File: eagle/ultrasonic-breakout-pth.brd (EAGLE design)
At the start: 58.7 x 41.9 mm, 25 parts, among them Q1 16 MHz, U1 ATMEGA328P_PDIP

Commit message: refining board layout
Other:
- board size 58.7 x 41.9 mm -> 57.5 x 41.9 mm
- board text added: "MISO"
- board text added: "MOSI"
- board text added: "SCK"
- board text added: "SS"
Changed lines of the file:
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@@
 <board>
 <plain>
-<wire x1="1.27" y1="36.83" x2="59.995" y2="36.83" width="0" layer="20"/>
-<wire x1="59.995" y1="36.83" x2="59.995" y2="78.73" width="0" layer="20"/>
-<wire x1="59.995" y1="78.73" x2="1.27" y2="78.73" width="0" layer="20"/>
+<wire x1="1.27" y1="36.83" x2="58.725" y2="36.83" width="0" layer="20"/>
+<wire x1="58.725" y1="36.83" x2="58.725" y2="78.73" width="0" layer="20"/>
+<wire x1="58.725" y1="78.73" x2="1.27" y2="78.73" width="0" layer="20"/>
 <wire x1="1.27" y1="78.73" x2="1.27" y2="36.83" width="0" layer="20"/>
 <hole x="3.81" y="76.2" drill="3.2"/>
 <hole x="3.81" y="39.37" drill="3.2"/>
-<hole x="57.785" y="39.37" drill="3.2"/>
+<hole x="54.61" y="39.37" drill="3.2"/>
 <hole x="55.245" y="76.2" drill="3.2"/>
 <text x="7.62" y="75.565" size="0.6096" layer="25" rot="R90">GND</text>
@@
 <text x="15.24" y="75.565" size="0.6096" layer="25" rot="R90">5V</text>
 <text x="17.78" y="76.835" size="1.016" layer="25" font="vector" ratio="10">HC-SR04 Breakout 1.0.1</text>
-<text x="54.61" y="40.005" size="1.016" layer="25" font="vector" ratio="10" rot="R180">Copyright 2016 Grove Enterprises LLC</text>
+<text x="50.8" y="40.005" size="1.016" layer="25" font="vector" ratio="10" rot="R180">Copyright 2016 Grove Enterprises LLC</text>
+<text x="57.15" y="55.245" size="0.6096" layer="25" rot="R90">5V</text>
+<text x="57.15" y="52.705" size="0.6096" layer="25" rot="R90">SCK</text>
+<text x="57.15" y="49.53" size="0.6096" layer="25" rot="R90">MISO</text>
+<text x="57.15" y="46.99" size="0.6096" layer="25" rot="R90">MOSI</text>
+<text x="57.15" y="45.085" size="0.6096" layer="25" rot="R90">SS</text>
+<text x="57.15" y="42.545" size="0.6096" layer="25" rot="R90">GND</text>
 </plain>
 <attributes>
@@
 <elements>
 <element name="ARDUINO" library="SparkFun-Connectors" package="1X06_LOCK" value="" x="54.61" y="43.18" smashed="yes" rot="R90">
-<attribute name="NAME" x="57.404" y="42.291" size="0.8128" layer="25" rot="R90"/>
+<attribute name="NAME" x="52.324" y="42.291" size="0.8128" layer="25" rot="R90"/>
 <attribute name="VALUE" x="57.404" y="51.181" size="1.27" layer="25" rot="R90"/>
 </element>

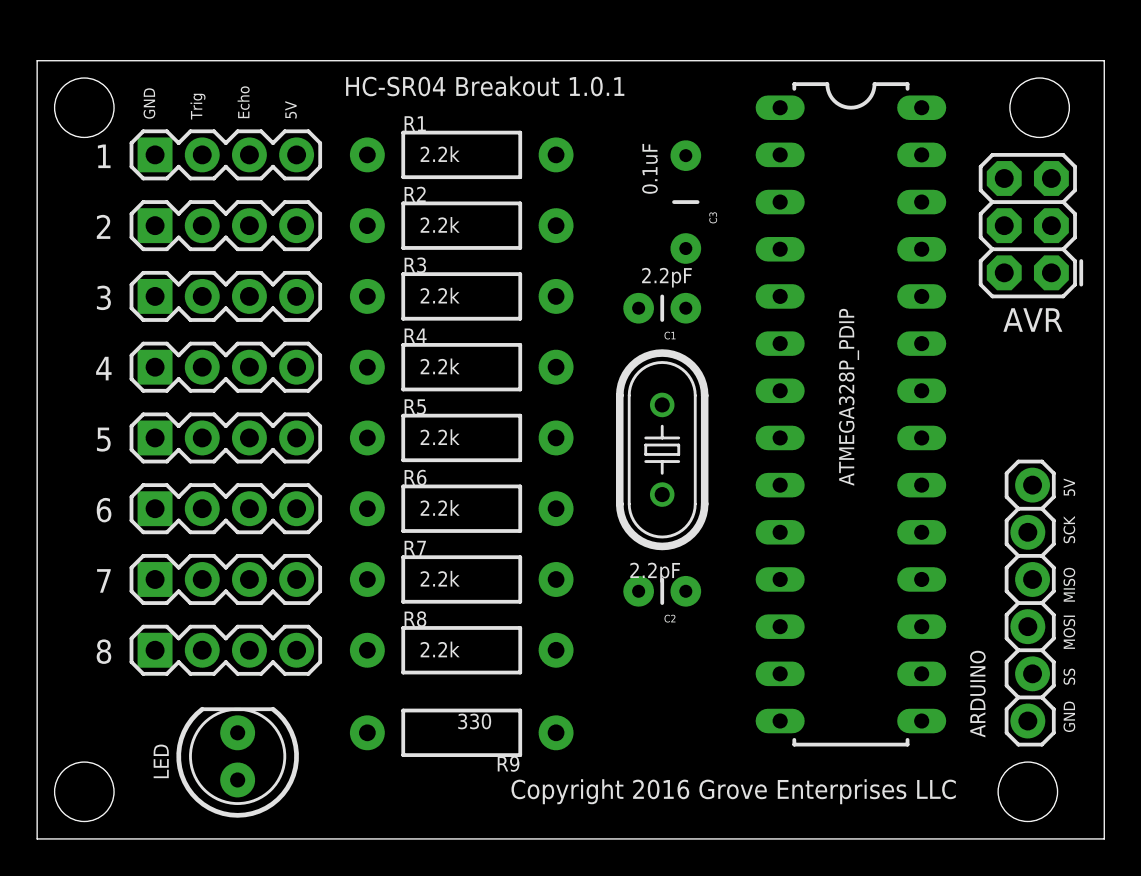
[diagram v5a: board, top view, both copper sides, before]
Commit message: changed first connecter to swap trig/echo
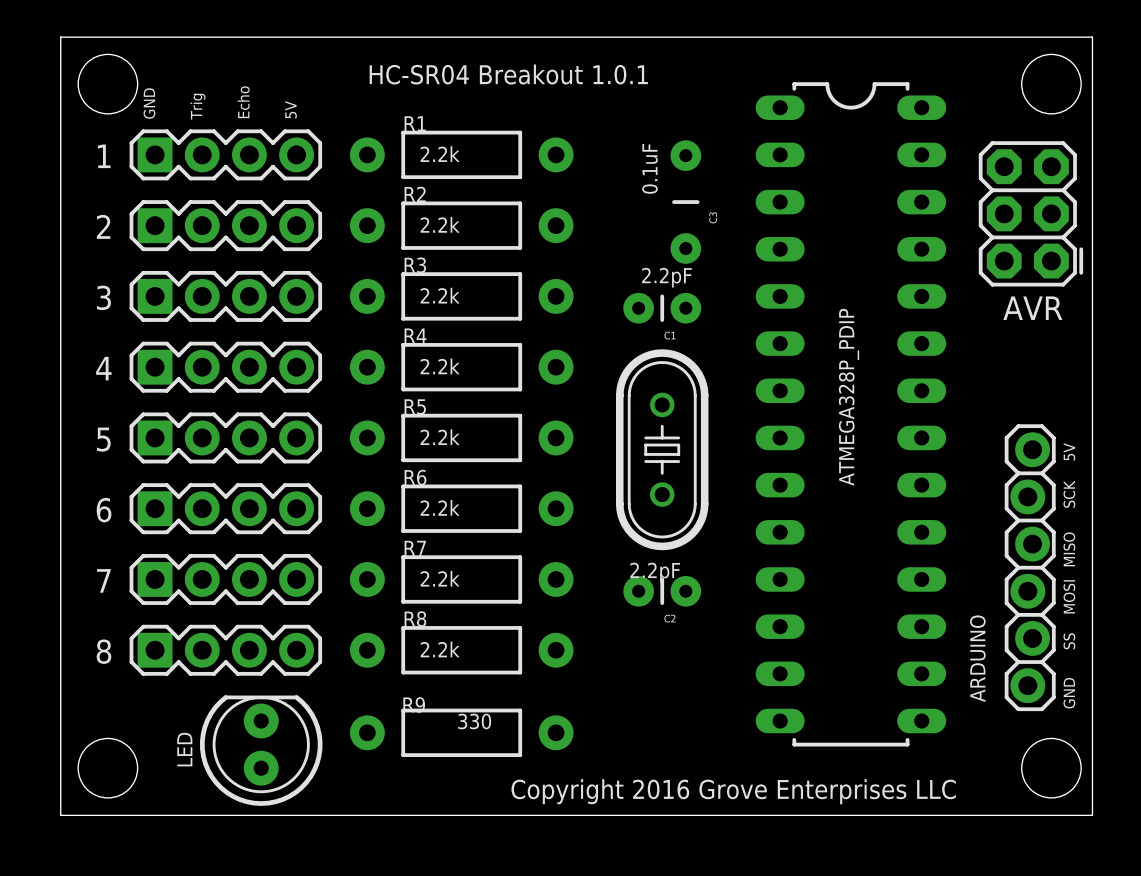
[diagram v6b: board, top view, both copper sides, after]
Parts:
- moved ARDUINO 1.91 mm to (54.6, 45.1)
- moved LED 1.42 mm to (13.3, 41.9)
- moved AVR 0.63 mm to (55.9, 67.9)
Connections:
- removed net TRIGGER1: 1.2, R1.P$1
- new net N$4: 1.3, R1.P$1
- net PD0: now also 1.2; no longer 1.3
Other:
- board size 57.5 x 41.9 mm -> 55.6 x 41.9 mm

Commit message: finished swapping trig/echo on all connectors
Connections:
- net N$10: now also 7.3; no longer 7.2
- net N$11: now also 8.3; no longer 8.2
- net N$5: now also 2.3; no longer 2.2
- net N$6: now also 3.3; no longer 3.2
- net N$7: now also 4.3; no longer 4.2
- net N$8: now also 5.3; no longer 5.2
- net N$9: now also 6.3; no longer 6.2
- net PD1: now also 2.2; no longer 2.3
- net PD2: now also 3.2; no longer 3.3
- net PD3: now also 4.2; no longer 4.3
- net PD4: now also 5.2; no longer 5.3
- net PD5: now also 6.2; no longer 6.3
- net PD6: now also 7.2; no longer 7.3
- net PD7: now also 8.2; no longer 8.3
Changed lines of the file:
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@@
 <hole x="55.88" y="77.47" drill="3.2"/>
 <text x="7.62" y="75.565" size="0.6096" layer="25" rot="R90">GND</text>
-<text x="10.16" y="75.565" size="0.6096" layer="25" rot="R90">Trig</text>
-<text x="12.7" y="75.565" size="0.6096" layer="25" rot="R90">Echo</text>
+<text x="12.7" y="75.565" size="0.6096" layer="25" rot="R90">Trig</text>
+<text x="10.16" y="75.565" size="0.6096" layer="25" rot="R90">Echo</text>
 <text x="15.24" y="75.565" size="0.6096" layer="25" rot="R90">5V</text>
 <text x="19.05" y="77.47" size="1.016" layer="25" font="vector" ratio="10">HC-SR04 Breakout 1.0.1</text>
@@
 <contactref element="2" pad="1"/>
 <contactref element="3" pad="1"/>
-<contactref element="4" pad="1"/>
 <contactref element="5" pad="1"/>
 <contactref element="6" pad="1"/>
@@
 <contactref element="C3" pad="2"/>
 <contactref element="LED" pad="K"/>
+<contactref element="4" pad="1"/>
 <wire x1="48.895" y1="60.96" x2="53.34" y2="73.025" width="0" layer="19" extent="1-1"/>
 <wire x1="41.275" y1="58.42" x2="48.895" y2="60.96" width="0" layer="19" extent="1-1"/>
@@
 <signal name="PD3">
 <contactref element="U1" pad="5"/>
-<contactref element="4" pad="3"/>
 <contactref element="R4" pad="P$2"/>
+<contactref element="4" pad="2"/>
 <wire x1="29.21" y1="62.23" x2="41.275" y2="66.04" width="0" layer="19" extent="1-1"/>
-<wire x1="12.7" y1="62.23" x2="29.21" y2="62.23" width="0" layer="19" extent="1-1"/>
+<wire x1="10.16" y1="62.23" x2="29.21" y2="62.23" width="0" layer="19" extent="1-1"/>
 </signal>
 <signal name="PD4">
 <contactref element="U1" pad="6"/>
-<contactref element="5" pad="3"/>
 <contactref element="R5" pad="P$2"/>
+<contactref element="5" pad="2"/>
 <wire x1="29.21" y1="58.42" x2="41.275" y2="63.5" width="0" layer="19" extent="1-1"/>
-<wire x1="12.7" y1="58.42" x2="29.21" y2="58.42" width="0" layer="19" extent="1-1"/>
+<wire x1="10.16" y1="58.42" x2="29.21" y2="58.42" width="0" layer="19" extent="1-1"/>
 </signal>
 <signal name="PD5">
 <contactref element="U1" pad="11"/>
-<contactref element="6" pad="3"/>
 <contactref element="R6" pad="P$2"/>
+<contactref element="6" pad="2"/>
 <wire x1="29.21" y1="54.61" x2="41.275" y2="50.8" width="0" layer="19" extent="1-1"/>
-<wire x1="12.7" y1="54.61" x2="29.21" y2="54.61" width="0" layer="19" extent="1-1"/>
+<wire x1="10.16" y1="54.61" x2="29.21" y2="54.61" width="0" layer="19" extent="1-1"/>
 </signal>
 <signal name="PD6">
 <contactref element="U1" pad="12"/>
-<contactref element="7" pad="3"/>
 <contactref element="R7" pad="P$2"/>
+<contactref element="7" pad="2"/>
 <wire x1="29.21" y1="50.8" x2="41.275" y2="48.26" width="0" layer="19" extent="1-1"/>
-<wire x1="12.7" y1="50.8" x2="29.21" y2="50.8" width="0" layer="19" extent="1-1"/>
+<wire x1="10.16" y1="50.8" x2="29.21" y2="50.8" width="0" layer="19" extent="1-1"/>
 </signal>
 <signal name="PD7">
 <contactref element="U1" pad="13"/>
-<contactref element="8" pad="3"/>
 <contactref element="R8" pad="P$2"/>
+<contactref element="8" pad="2"/>
 <wire x1="29.21" y1="46.99" x2="41.275" y2="45.72" width="0" layer="19" extent="1-1"/>
-<wire x1="12.7" y1="46.99" x2="29.21" y2="46.99" width="0" layer="19" extent="1-1"/>
+<wire x1="10.16" y1="46.99" x2="29.21" y2="46.99" width="0" layer="19" extent="1-1"/>
 </signal>
 <signal name="PD1">
 <contactref element="U1" pad="3"/>
-<contactref element="2" pad="3"/>
 <contactref element="R2" pad="P$2"/>
+<contactref element="2" pad="2"/>
 <wire x1="29.21" y1="69.85" x2="41.275" y2="71.12" width="0" layer="19" extent="1-1"/>
-<wire x1="12.7" y1="69.85" x2="29.21" y2="69.85" width="0" layer="19" extent="1-1"/>
+<wire x1="10.16" y1="69.85" x2="29.21" y2="69.85" width="0" layer="19" extent="1-1"/>
 </signal>
 <signal name="PD2">
 <contactref element="U1" pad="4"/>
-<contactref element="3" pad="3"/>
 <contactref element="R3" pad="P$2"/>
+<contactref element="3" pad="2"/>
 <wire x1="29.21" y1="66.04" x2="41.275" y2="68.58" width="0" layer="19" extent="1-1"/>
-<wire x1="12.7" y1="66.04" x2="29.21" y2="66.04" width="0" layer="19" extent="1-1"/>
-</signal>
-<signal name="N$5">
-<contactref element="2" pad="2"/>
-<contactref element="R2" pad="P$1"/>
-<wire x1="10.16" y1="69.85" x2="19.05" y2="69.85" width="0" layer="19" extent="1-1"/>
-</signal>
-<signal name="N$6">
-<contactref element="3" pad="2"/>
-<contactref element="R3" pad="P$1"/>
-<wire x1="10.16" y1="66.04" x2="19.05" y2="66.04" width="0" layer="19" extent="1-1"/>
-</signal>
-<signal name="N$7">
-<contactref element="4" pad="2"/>
-<contactref element="R4" pad="P$1"/>
-<wire x1="10.16" y1="62.23" x2="19.05" y2="62.23" width="0" layer="19" extent="1-1"/>
-</signal>
-<signal name="N$8">
-<contactref element="5" pad="2"/>
-<contactref element="R5" pad="P$1"/>
-<wire x1="10.16" y1="58.42" x2="19.05" y2="58.42" width="0" layer="19" extent="1-1"/>
-</signal>
-<signal name="N$9">
-<contactref element="6" pad="2"/>
-<contactref element="R6" pad="P$1"/>
-<wire x1="10.16" y1="54.61" x2="19.05" y2="54.61" width="0" layer="19" extent="1-1"/>
-</signal>
-<signal name="N$10">
-<contactref element="7" pad="2"/>
-<contactref element="R7" pad="P$1"/>
-<wire x1="10.16" y1="50.8" x2="19.05" y2="50.8" width="0" layer="19" extent="1-1"/>
-</signal>
-<signal name="N$11">
-<contactref element="8" pad="2"/>
-<contactref element="R8" pad="P$1"/>
-<wire x1="10.16" y1="46.99" x2="19.05" y2="46.99" width="0" layer="19" extent="1-1"/>
+<wire x1="10.16" y1="66.04" x2="29.21" y2="66.04" width="0" layer="19" extent="1-1"/>
 </signal>
 <signal name="N$12">
@@
 <wire x1="12.7" y1="73.66" x2="19.05" y2="73.66" width="0" layer="19" extent="1-1"/>
 </signal>
+<signal name="N$5">
+<contactref element="2" pad="3"/>
+<contactref element="R2" pad="P$1"/>
+<wire x1="12.7" y1="69.85" x2="19.05" y2="69.85" width="0" layer="19" extent="1-1"/>
+</signal>
+<signal name="N$6">
+<contactref element="3" pad="3"/>
+<contactref element="R3" pad="P$1"/>
+<wire x1="12.7" y1="66.04" x2="19.05" y2="66.04" width="0" layer="19" extent="1-1"/>
+</signal>
+<signal name="N$7">
+<contactref element="4" pad="3"/>
+<contactref element="R4" pad="P$1"/>
+<wire x1="12.7" y1="62.23" x2="19.05" y2="62.23" width="0" layer="19" extent="1-1"/>
+</signal>
+<signal name="N$8">
+<contactref element="5" pad="3"/>
+<contactref element="R5" pad="P$1"/>
+<wire x1="12.7" y1="58.42" x2="19.05" y2="58.42" width="0" layer="19" extent="1-1"/>
+</signal>
+<signal name="N$9">
+<contactref element="6" pad="3"/>
+<contactref element="R6" pad="P$1"/>
+<wire x1="12.7" y1="54.61" x2="19.05" y2="54.61" width="0" layer="19" extent="1-1"/>
+</signal>
+<signal name="N$10">
+<contactref element="7" pad="3"/>
+<contactref element="R7" pad="P$1"/>
+<wire x1="12.7" y1="50.8" x2="19.05" y2="50.8" width="0" layer="19" extent="1-1"/>
+</signal>
+<signal name="N$11">
+<contactref element="8" pad="3"/>
+<contactref element="R8" pad="P$1"/>
+<wire x1="12.7" y1="46.99" x2="19.05" y2="46.99" width="0" layer="19" extent="1-1"/>
+</signal>
 </signals>

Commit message: Fix error on board (AVR ISP did not have SCK routed)
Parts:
- moved 1 0.64 mm to (8.26, 73.7)
- moved 2 0.64 mm to (8.26, 69.8)
- moved 3 0.64 mm to (8.26, 66.0)
- moved 4 0.64 mm to (8.26, 62.2)
- moved 5 0.64 mm to (8.26, 58.4)
- moved 6 0.64 mm to (8.26, 54.6)
- moved 7 0.64 mm to (8.26, 50.8)
- moved 8 0.64 mm to (8.26, 47.0)
- moved C1 0.63 mm to (35.6, 65.4)
- moved C2 0.63 mm to (35.6, 50.2)
- moved C3 0.63 mm to (35.6, 71.1)
- moved Q1 0.63 mm to (34.3, 57.8)
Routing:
- net GND: track 0.00 -> 130.6 mm
- net 5V: track 0.00 -> 89.0 mm
- net PD4: track 0.00 -> 34.4 mm
- net PD6: track 0.00 -> 34.1 mm
- net PD0: track 0.00 -> 33.3 mm
- net PD3: track 0.00 -> 33.1 mm
- net PD5: track 0.00 -> 33.1 mm
- net PD2: track 0.00 -> 32.6 mm
- net PD1: track 0.00 -> 32.1 mm
- net PD7: track 0.00 -> 32.1 mm
- net MOSI: track 0.00 -> 28.4 mm
- net SCK: track 0.00 -> 23.3 mm
- net MISO: track 0.00 -> 23.2 mm
- net N$2: track 0.00 -> 15.9 mm
- net N$1: track 0.00 -> 14.8 mm
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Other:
- board size 55.6 x 41.9 mm -> 54.9 x 41.9 mm
